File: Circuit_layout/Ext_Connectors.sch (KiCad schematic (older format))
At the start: 12 parts, among them CON1 AVR-JTAG-10, J1 Spare_Conns, J4 Motor_Ctrl, J5 RJ12, P1 TSV, P2 CONN_02X10, P3 CONN_02X07, U14 Mounting_hole, U15 Mounting_hole, U25 Mounting_hole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

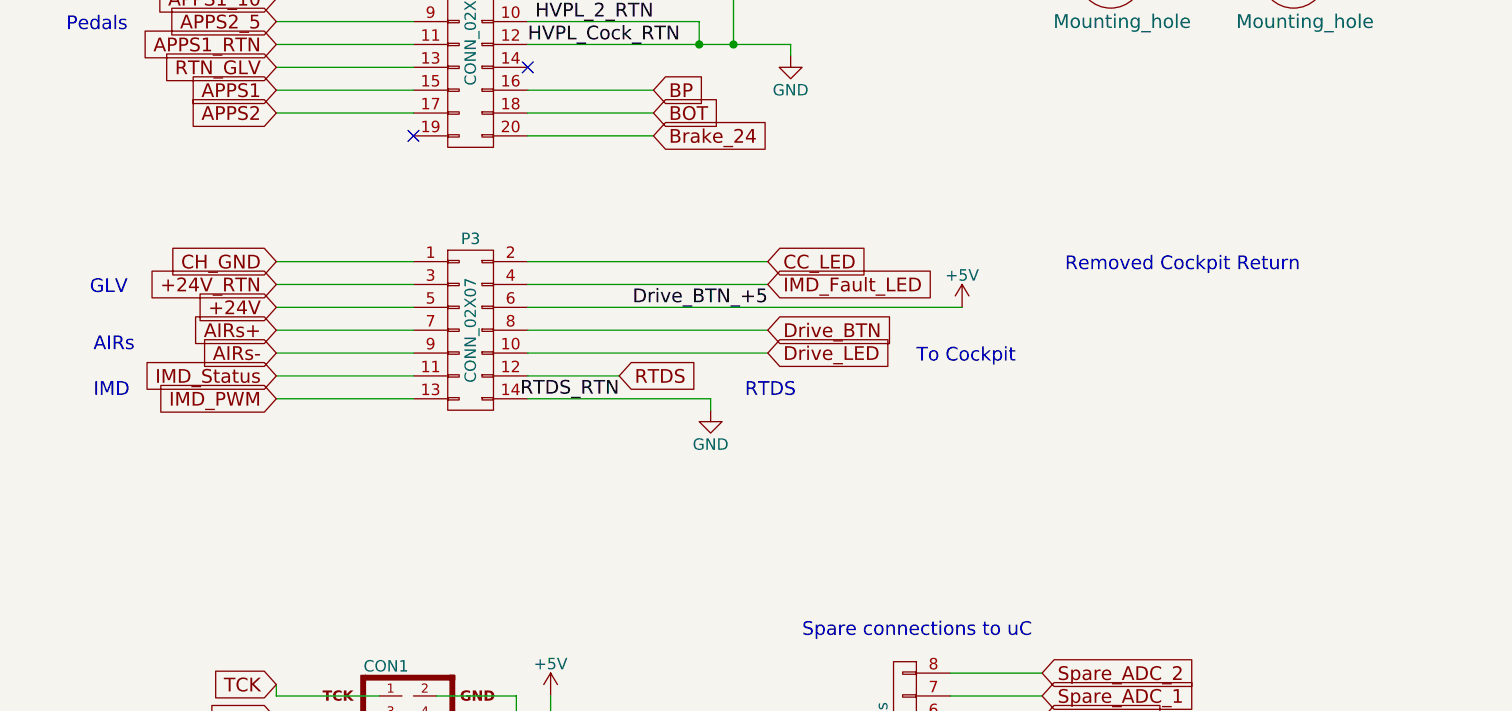
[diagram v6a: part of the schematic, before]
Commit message: Added comments to schematic to aid future years in understanding what went wrong and where
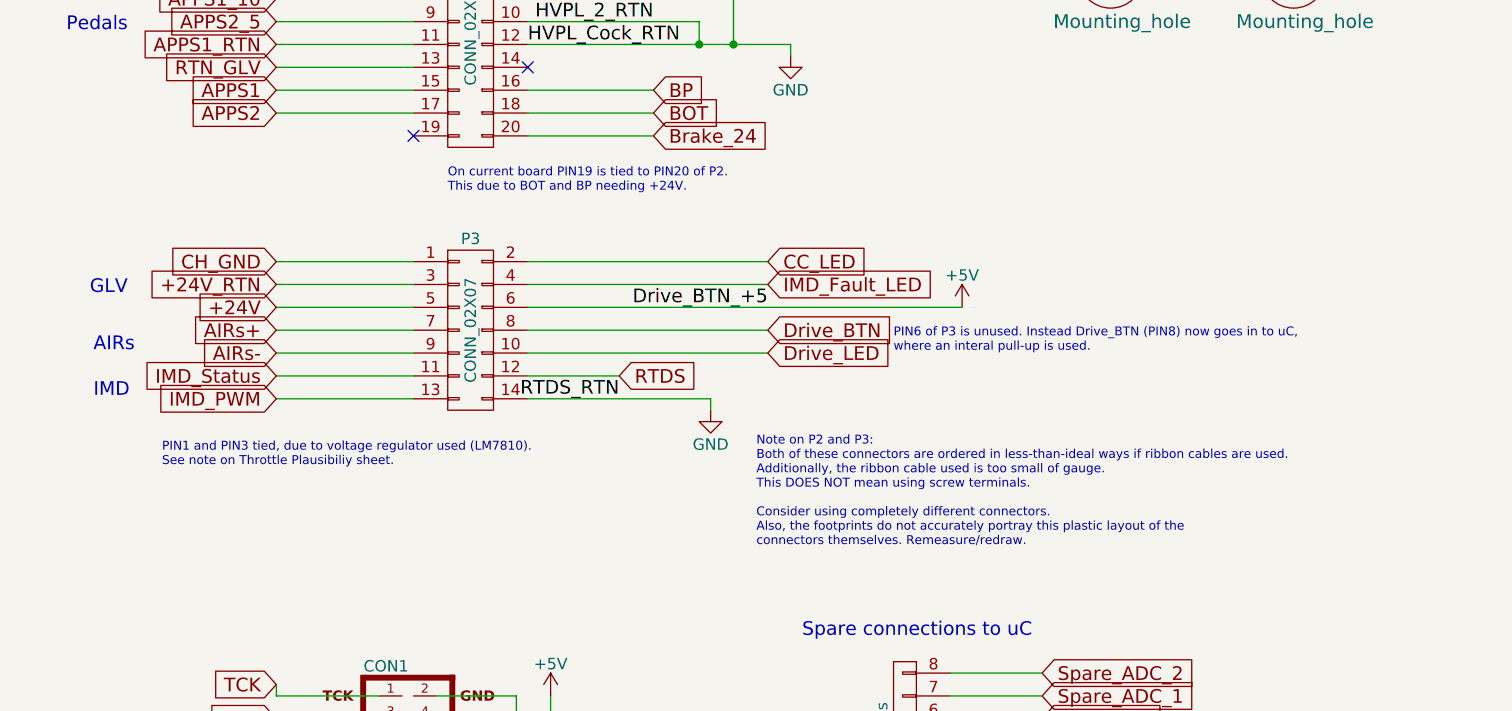
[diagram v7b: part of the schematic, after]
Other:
- note added: "Note on P2 and P3:\nBoth of these connectors are ordered in less-than-ideal ways if ribbon cables are used.\nAdditionally, the ribbon cable used is too small of gauge.\nThis DOES NOT mean using screw terminals.\n\nConsider using completely different connectors.\nAlso, the footprints do not accurately portray this plastic layout of the\nconnectors themselves. Remeasure/redraw."
- note added: "On current board PIN19 is tied to PIN20 of P2. \nThis due to BOT and BP needing +24V."
- note added: "PIN1 and PIN3 tied, due to voltage regulator used (LM7810).\nSee note on Throttle Plausibiliy sheet."
- note added: "PIN6 of P3 is unused. Instead Drive_BTN (PIN8) now goes in to uC,\nwhere an interal pull-up is used."
- note removed: "RTDS"
- note removed: "Removed Cockpit Return"
- note removed: "To Cockpit"
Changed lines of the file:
@@
 LIBS:xilinx
 LIBS:Zilog
-LIBS:pacman-main-cache
 LIBS:bss84
 LIBS:+10v
@@
 Text Label 7250 1050 2    60   ~ 0
 HVPL_1
-Text Notes 8400 2950 0    60   ~ 0
-To Cockpit
 Text Label 7250 1350 2    60   ~ 0
 HVPL_1_RTN
@@
 Text GLabel 7250 1750 2    60   Input ~ 0
 BP
-Text Notes 7650 3100 0    60   ~ 0
-RTDS
 $Comp
 L GND #PWR035
@@
 	1    0    0    -1
 $EndComp
-Text Notes 9050 2550 0    60   ~ 0
-Removed Cockpit Return
 Text GLabel 7750 2500 2    60   Input ~ 0
 CC_LED
 Wire Wire Line
 	7750 2500 6700 2500
+Text Notes 8300 2900 0    39   ~ 0
+PIN6 of P3 is unused. Instead Drive_BTN (PIN8) now goes in to uC,\nwhere an interal pull-up is used.
+Text Notes 6350 2200 0    39   ~ 0
+On current board PIN19 is tied to PIN20 of P2. \nThis due to BOT and BP needing +24V.
+Text Notes 5100 3400 0    39   ~ 0
+PIN1 and PIN3 tied, due to voltage regulator used (LM7810).\nSee note on Throttle Plausibiliy sheet.
+Text Notes 7700 3750 0    39   ~ 0
+Note on P2 and P3:\nBoth of these connectors are ordered in less-than-ideal ways if ribbon cables are used.\nAdditionally, the ribbon cable used is too small of gauge.\nThis DOES NOT mean using screw terminals.\n\nConsider using completely different connectors.\nAlso, the footprints do not accurately portray this plastic layout of the\nconnectors themselves. Remeasure/redraw.
 $EndSCHEMATC
